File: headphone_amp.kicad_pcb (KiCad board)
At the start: 2 copper layers, 88 parts, among them J1 USB4085-GF-A, J2 JST PH2, J3 JST GH2, J4 JST SH3, J5 Header_2x1, J6 JST SH3, J7 415-47-208-41-004000, J8 SJ-3523-SMT-TR, Q1 BSS138, SW1 SW_SPST, U1 BQ24074RGTR, U2 OPA1678, U3 OPA1622, U4 TLE2426xD, U5 TPS61379QWRTERQ1, U9 TLV7A0325PDBVR

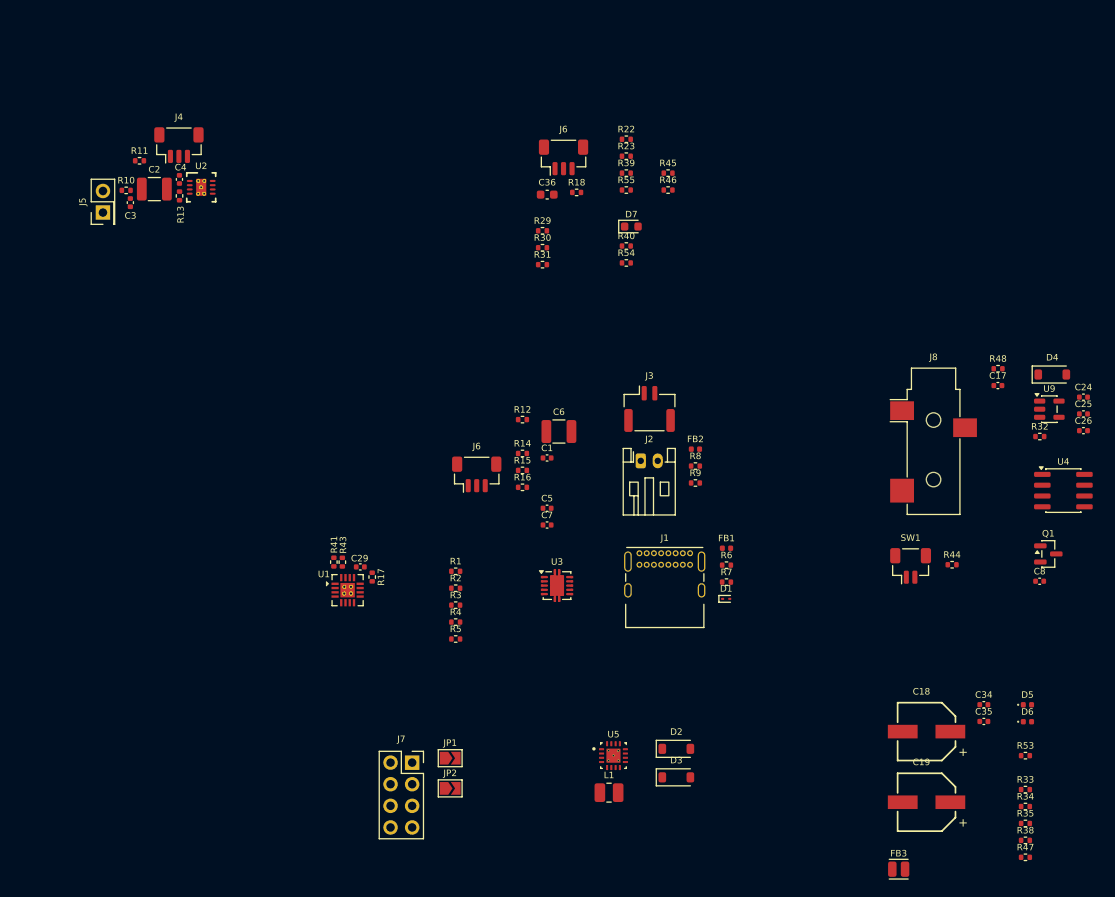
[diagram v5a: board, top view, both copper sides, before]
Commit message: Preliminary layout complete, done on airpane so needs verification.
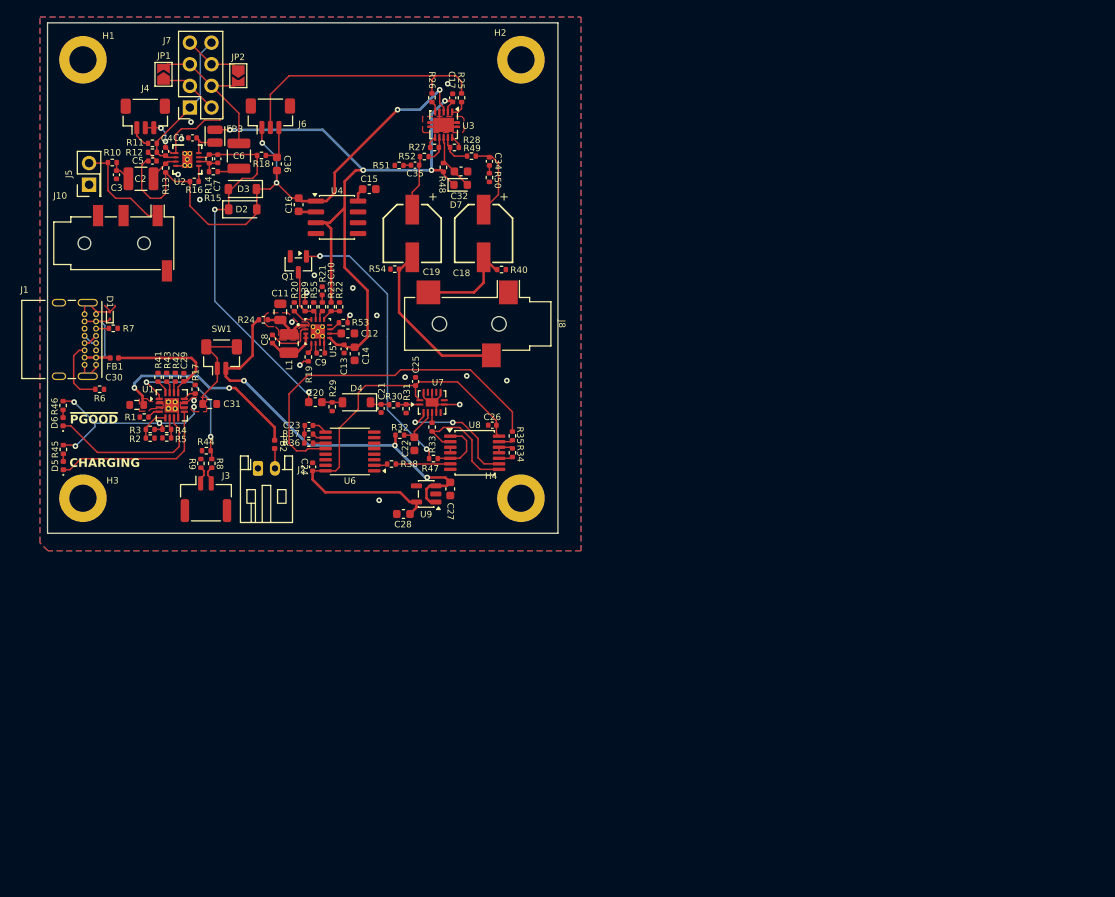
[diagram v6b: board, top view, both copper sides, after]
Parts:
- removed the J6 at (96.4, 82.4)
- added C10: 10nF, Capacitor_SMD:C_0402_1005Metric, F.Cu at (78.3, 60.8)
- added C11: 10uF, Capacitor_SMD:C_0805_2012Metric, F.Cu at (73.3, 63.3)
- added C12: 1.5uF, Capacitor_SMD:C_0603_1608Metric, F.Cu at (81.3, 65.8)
- added C13: 1uF, Capacitor_SMD:C_0402_1005Metric, F.Cu at (80.8, 67.7)
- added C14: 4.7uF, Capacitor_SMD:C_0603_1608Metric, F.Cu at (82.1, 68.2)
- added C15: 1uF, Capacitor_SMD:C_0603_1608Metric, F.Cu at (83.8, 48.9)
- added C16: 2.2uF, Capacitor_SMD:C_0603_1608Metric, F.Cu at (75.5, 50.7)
- added C20: 1uF, Capacitor_SMD:C_0603_1608Metric, F.Cu at (77.5, 73.9)
- added C21: 0.22uF, Capacitor_SMD:C_0402_1005Metric, F.Cu at (85.2, 74.7)
- added C22: 4.7uF, Capacitor_SMD:C_0603_1608Metric, F.Cu at (89.1, 78.8)
- added C23: 0.68uF, Capacitor_SMD:C_0402_1005Metric, F.Cu at (76.7, 76.7)
- added C27: 2.2uF, Capacitor_SMD:C_0603_1608Metric, F.Cu at (93.3, 84.1)
- added C28: 2.2uF, Capacitor_SMD:C_0603_1608Metric, F.Cu at (87.8, 87.1)
- added C30: 4.7uF, Resistor_SMD:R_0603_1608Metric, F.Cu at (56.5, 74.2)
- added C31: 4.7uF, Resistor_SMD:R_0603_1608Metric, F.Cu at (65.0, 74.1)
- added C32: 2.2uF, Capacitor_SMD:C_0603_1608Metric, F.Cu at (94.6, 46.8)
- added C9: 1uF, Capacitor_SMD:C_0402_1005Metric, F.Cu at (78.1, 68.2)
- added H1: MountingHole_Pad, MountingHole:MountingHole_3.2mm_M3_DIN965_Pad, F.Cu at (50.1, 33.7)
- added H2: MountingHole_Pad, MountingHole:MountingHole_3.2mm_M3_DIN965_Pad, F.Cu at (101.6, 33.7)
- added H3: MountingHole_Pad, MountingHole:MountingHole_3.2mm_M3_DIN965_Pad, F.Cu at (50.1, 85.2)
- added H4: MountingHole_Pad, MountingHole:MountingHole_3.2mm_M3_DIN965_Pad, F.Cu at (101.6, 85.2)
- added J10: AudioJack2, Connector_Audio:Jack_3.5mm_PJ320D_Horizontal, F.Cu at (55.1, 55.2)
- added R19: 0R, Resistor_SMD:R_0402_1005Metric, F.Cu at (76.6, 68.6)
- added R20: 18K, Resistor_SMD:R_0402_1005Metric, F.Cu at (75.0, 62.7)
- added R21: 56.2K, Resistor_SMD:R_0402_1005Metric, F.Cu at (78.3, 62.7)
- added R24: 0R, Resistor_SMD:R_0402_1005Metric, F.Cu at (71.3, 64.2)
- added R25: 0R, Resistor_SMD:R_0402_1005Metric, F.Cu at (94.6, 38.1)
- added R26: 0R, Resistor_SMD:R_0402_1005Metric, F.Cu at (91.2, 38.1)
- added R27: 0R, Resistor_SMD:R_0402_1005Metric, F.Cu at (91.5, 44.0)
- added R28: 0R, Resistor_SMD:R_0402_1005Metric, F.Cu at (93.8, 44.0)
- added R36: 220K, Resistor_SMD:R_0402_1005Metric, F.Cu at (76.7, 78.7)
- added R37: 100K, Resistor_SMD:R_0402_1005Metric, F.Cu at (76.7, 77.7)
- added R42: 46.4K, Resistor_SMD:R_0402_1005Metric, F.Cu at (61.0, 71.0)
- added R49: 0R, Resistor_SMD:R_0402_1005Metric, F.Cu at (95.8, 45.0)
- added R50: 0R, Resistor_SMD:R_0402_1005Metric, F.Cu at (97.9, 47.5)
- added R51: 0R, Resistor_SMD:R_0402_1005Metric, F.Cu at (87.3, 46.1)
- added R52: 0R, Resistor_SMD:R_0402_1005Metric, F.Cu at (90.3, 45.1)
- added U6: CD74HC4060, Package_SO:TSSOP-16_4.4x5mm_P0.65mm, F.Cu at (81.5, 79.7)
- added U7: 74HC14BQ,115, Package_DFN_QFN:DHVQFN-14-1EP_2.5x3mm_P0.5mm_EP1x1.5mm, F.Cu at (91.2, 74.0)
- added U8: 74HC02, Package_SO:TSSOP-14_4.4x5mm_P0.65mm, F.Cu at (96.2, 79.9)
- moved D6 118.7 mm to (47.8, 76.2), turned to 90 degrees
- moved FB3 117.8 mm to (65.7, 42.7), turned to -90 degrees
- moved D5 116.8 mm to (47.8, 81.4), turned to 90 degrees
- moved R53 95.0 mm to (80.7, 64.6)
- moved C8 94.6 mm to (72.4, 66.5), turned to -90 degrees
- moved Q1 94.5 mm to (75.5, 57.7), turned to -90 degrees
- moved C35 93.5 mm to (89.2, 46.1)
- moved U4 91.2 mm to (80.0, 52.2)
- moved C24 91.0 mm to (77.1, 81.5), turned to 90 degrees
- moved C19 90.1 mm to (88.8, 54.1), turned to 90 degrees
- moved R44 88.7 mm to (64.6, 79.6), turned to 180 degrees
- moved JP2 87.4 mm to (68.4, 35.5), turned to -90 degrees
- moved JP1 87.2 mm to (59.6, 35.4), turned to 90 degrees
- moved R38 86.7 mm to (86.4, 81.2), turned to 180 degrees
- moved C34 86.4 mm to (97.9, 45.6), turned to 90 degrees
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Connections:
- net Net-(J3-Pin_2) renamed /Battery/S_T+
- net Net-(U2B-+) renamed /Audio Input/SECOND_STAGE_P
- J3 pad 1: GND -> /Battery/S_T-
- J4 pad 1: /Audio Input/FIRST_STAGE_OUT -> /Audio Input/FB_RES
- J4 pad 3: /Audio Input/FB_RES -> /Audio Input/FIRST_STAGE_OUT
- R9 pad 1: GND -> /Battery/S_T-
- U2 pad 9: (no net) -> GND
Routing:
- net /V+: track 0.00 -> 84.6 mm, vias 0 -> 4
- net /V_{MID}: track 0.00 -> 69.2 mm, vias 0 -> 4
- net /Watchdog/V_{LOGIC}: track 0.00 -> 51.6 mm
- net /V_{SYS}: track 0.00 -> 47.7 mm, vias 0 -> 3
- net /WD_AUDIO_IN: track 0.00 -> 44.8 mm, vias 0 -> 2
- net /Watchdog/WAKE: track 0.00 -> 42.4 mm
- net /Battery Charger/OUT: track 0.00 -> 36.5 mm, vias 0 -> 5
- net /Audio Input/FIRST_STAGE_OUT: track 0.00 -> 35.1 mm, vias 0 -> 2
- net /SHUTDOWN: track 0.00 -> 32.8 mm, vias 0 -> 2
- net GND: track 0.00 -> 31.8 mm, vias 0 -> 13
- net /AUDIO_BUFFER_IN: track 0.00 -> 31.2 mm
- net /V_{BAT}: track 0.00 -> 23.9 mm, vias 0 -> 2
- net /Current Buffer/HEADPHONES_RIGHT: track 0.00 -> 20.2 mm
- net /Battery Charger/~{CHG}: track 0.00 -> 19.7 mm
- net /Battery Charger/~{PGOOD}: track 0.00 -> 18.8 mm
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- added copper zone on F.Cu, net /Battery Charger/OUT
- added copper zone on F.Cu, net /Boost/Vin
- added copper zone on In2.Cu, net /Boost/Vin
- added copper zone on F.Cu, net /V_{BAT}
- added copper zone on B.Cu, net GND
- added copper zone on F.Cu, net GND
- added copper zone on In1.Cu, net GND
- added copper zone on In2.Cu, net GND
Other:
- board outline added: 60 x 60 mm
- copper layers 2 -> 4
- board text added: "CHARGING"
- board text added: "~{PGOOD}"

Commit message: Started adding some 3D models and footprints.
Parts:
- J10: footprint Connector_Audio:Jack_3.5mm_PJ320D_Horizontal -> connectors:CONN_MJ-3523_CUD
- moved J10 2.09 mm to (53.7, 53.6)
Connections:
- J1 pad A8: (no net) -> unconnected-(J1-SBU1-PadA8)
- J1 pad B8: (no net) -> unconnected-(J1-SBU2-PadB8)
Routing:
- net /Audio Input/JACK_IN: track 12.6 -> 16.6 mm

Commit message: Added via stitching.
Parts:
- added FID1: Fiducial, Fiducial:Fiducial_1.5mm_Mask3mm, B.Cu at (60.4, 82.9)
- added FID2: Fiducial, Fiducial:Fiducial_1.5mm_Mask3mm, B.Cu at (83.9, 35.1)
- added FID3: Fiducial, Fiducial:Fiducial_1.5mm_Mask3mm, B.Cu at (100.6, 74.4)
- added FID4: Fiducial, Fiducial:Fiducial_1.5mm_Mask3mm, F.Cu at (57.3, 85.5)
- added FID5: Fiducial, Fiducial:Fiducial_1.5mm_Mask3mm, F.Cu at (100.4, 41.4)
- added FID6: Fiducial, Fiducial:Fiducial_1.5mm_Mask3mm, F.Cu at (59.0, 63.0)
- J8: footprint Connector_Audio:Jack_3.5mm_CUI_SJ-3523-SMT_Horizontal -> connectors:Jack_3.5mm_CUI_SJ-3523-SMT_Horizontal
- U7: footprint Package_DFN_QFN:DHVQFN-14-1EP_2.5x3mm_P0.5mm_EP1x1.5mm -> integrated_circuits:DHVQFN14_SOT762-1_NEX
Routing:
- net /V_{BAT}: track 23.9 -> 20.3 mm
- net /Battery Charger/OUT: track 36.5 -> 37.2 mm
- net GND: vias 13 -> 131
